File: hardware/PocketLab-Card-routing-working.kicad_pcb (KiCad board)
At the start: 4 copper layers, 85.6 x 54 mm, 260 parts, among them J1 USB-C DATA/POWER, J2 microSD, J3 EXTERNAL 400uH LF COIL, J4 PROTECTED 1S LiPo 3.7V, J5 30-PIN 2.54mm DUPONT GRID, Q1 AO3400A IR DRIVER, Q2 CSD16406Q3 DISCHARGE, Q3 CSD16406Q3 CHARGE, SW1 RESET, SW2 BOOT, SW3 UP, SW4 DOWN, SW5 MAIN POWER OFF / ON, SW6 PAIR, SW7 SELECT, SW8 AUX CONFIG, U1 ESP32-S3-WROOM-1-N8R2, U10 BMI270 (FULL OPTION), U11 BMP390 (FULL OPTION), U12 PCF8563T, U13 TSOP75338WTR 38kHz, U14 BQ29700DSE, U15 TPS2553DBVR 500mA LIMIT, U16 USBLC6-4SC6Y, U17 TPS22919DCKR LF 5V LOAD SWITCH, U18 TCA9534PWR INTERNAL CONTROL, U19 SRV05-4MR6T1G SD ESD, U2 PN5321A3HN/C106, U20 SN74AHCT1G126DBVR RGB LEVEL S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, U21 SN74LV125ATPWR LF/SPI 3V3-TO-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, U22 SN74LVC1G126DBVR LF 5V-TO-3V3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, U23 ATECC608C-SSHDA-T, U24 SRV05-4MR6T1G J5 BUS ESD, U25 SRV05-4MR6T1G J5 SPI ESD, U3 E07-900MM10S 855-925MHz, U4 HTRC11001T/03EE,11 125kHz, U5 BQ24074RGTR, U6 TPS63070RNMR 3V3, U7 TPS61023DRLR 5V BOOST, U8 MAX17048G+T10, U9 TCA9535PWR, Y301 27.12MHz crystal (pins 2/4 sh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, Y501 4MHz 5V CMOS OSCILLATOR, Y701 32.768kHz CL=7pF

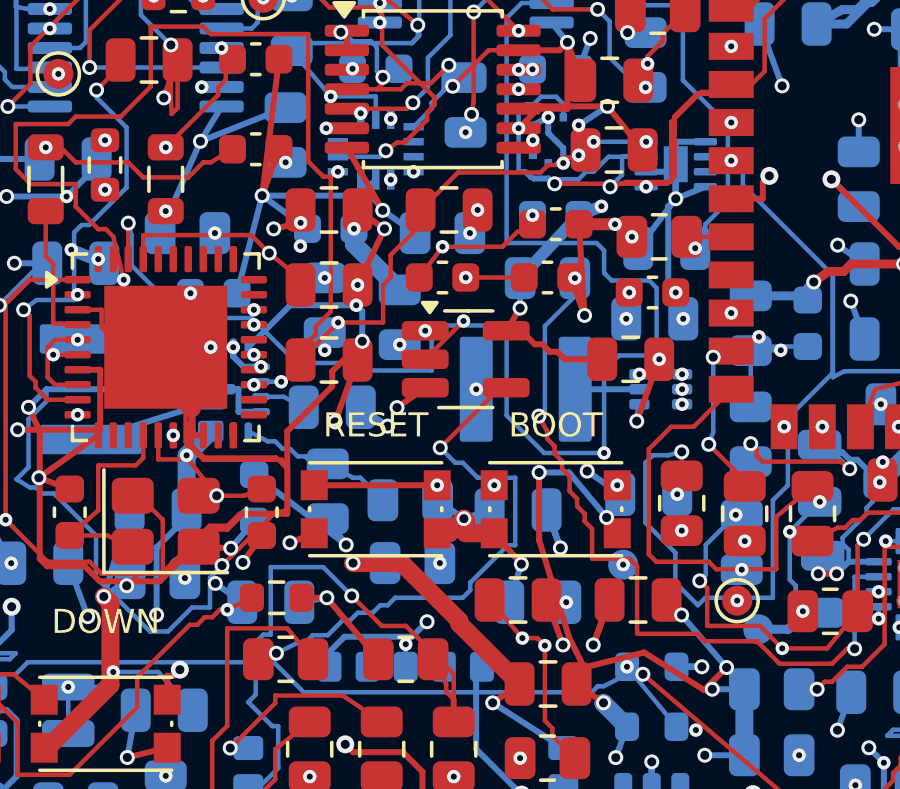
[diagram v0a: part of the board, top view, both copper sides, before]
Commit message: Reduce routing conflicts around power and control nets
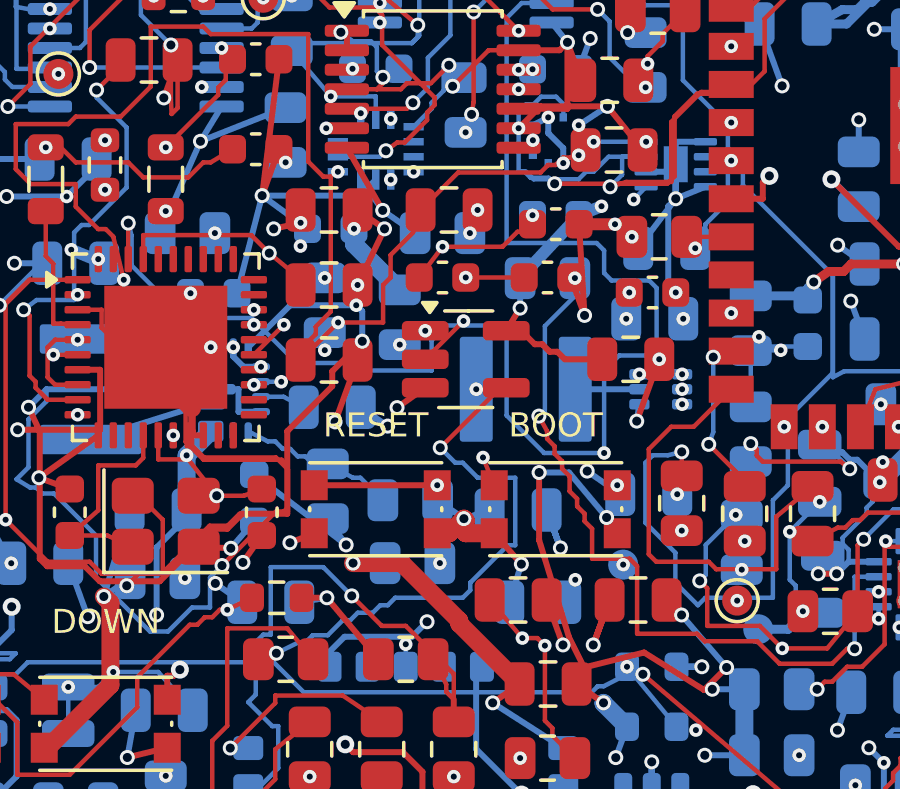
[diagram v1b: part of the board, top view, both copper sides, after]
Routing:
- net /BQ_EN1: track 47.3 -> 58.1 mm
- net /BOARD_TEMP_HDR: track 74.7 -> 78.7 mm
- net /BOOT_N: track 76.7 -> 78.6 mm
- net /+5V_RAW: track 227.8 -> 229.0 mm
- net /FG_ALERT_N: track 25.1 -> 26.1 mm
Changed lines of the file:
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@@
 	)
 	(via
-		(at 78.35 51.1)
+		(at 78.65 50.35)
 		(size 0.45)
 		(drill 0.2)
@@
 	)
 	(segment
-		(start 78.35 51.1)
+		(start 78.65 50.35)
 		(end 82.6715 55.3622)
 		(width 0.4)
@@
 	)
 	(segment
+		(start 78.35 51.1)
+		(end 78.65 50.35)
+		(width 0.4)
+		(locked yes)
+		(layer "B.Cu")
+		(net "/+5V_RAW")
+	)
+	(segment
 		(start 49.4104 59.75)
 		(end 48.4557 60.7047)
@@
 		(width 0.15)
 		(locked yes)
-		(layer "In1.Cu")
+		(layer "In2.Cu")
 		(net "/ESP_EN")
 	)
@@
 		(net "/I2C_SCL")
 	)
+	(segment
+		(start 67.9375 42.85)
+		(end 68.9375 41.85)
+		(width 0.15)
+		(layer "F.Cu")
+		(net "/NFC_IRQ_N")
+	)
 	(via
 		(at 83.85 35.11)
@@
 	)
 	(via
-		(at 67.9375 42.85)
+		(at 68.9375 41.85)
 		(size 0.45)
 		(drill 0.2)
@@
 	)
 	(segment
-		(start 67.9375 42.85)
+		(start 68.9375 41.85)
 		(end 83.85 35.11)
 		(width 0.15)
@@
 	)
 	(via
-		(at 75.95 47.2)
+		(at 75.575 46.275)
 		(size 0.45)
 		(drill 0.2)
@@
 	)
 	(segment
-		(start 75.95 47.2)
+		(start 75.575 46.275)
 		(end 75.95 62)
 		(width 0.15)
@@
 	)
 	(segment
+		(start 75.95 47.2)
+		(end 75.575 46.275)
+		(width 0.15)
+		(locked yes)
+		(layer "F.Cu")
+		(net "/BOOT_N")
+	)
+	(segment
 		(start 66.2 65.7125)
 		(end 65.65 65.7125)
@@
 	)
 	(segment
-		(start 59.2 23.2)
+		(start 61.2 52.8)
 		(end 59.2 52.8)
 		(width 0.15)
@@
 	)
 	(segment
+		(start 61.2 23.2)
+		(end 61.2 52.8)
+		(width 0.15)
+		(locked yes)
+		(layer "In2.Cu")
+		(net "/BOARD_TEMP_HDR")
+	)
+	(segment
+		(start 59.2 23.2)
+		(end 61.2 23.2)
+		(width 0.15)
+		(locked yes)
+		(layer "In2.Cu")
+		(net "/BOARD_TEMP_HDR")
+	)
+	(segment
 		(start 30.575 21.82)
 		(end 30.575 23.2)
@@
 	(segment
 		(start 88.7625 50.75)
+		(end 90 50.75)
+		(width 0.15)
+		(locked yes)
+		(layer "In2.Cu")
+		(net "/BQ_EN1")
+	)
+	(segment
+		(start 90 50.75)
+		(end 90 29.175)
+		(width 0.15)
+		(locked yes)
+		(layer "In2.Cu")
+		(net "/BQ_EN1")
+	)
+	(segment
+		(start 90 29.175)
 		(end 77.8625 29.175)
 		(width 0.15)
@@
 	)
 	(via
-		(at 81.0125 37.25)
+		(at 80.6 37.675)
 		(size 0.45)
 		(drill 0.2)
@@
 	)
 	(segment
-		(start 81.0125 37.25)
+		(start 80.6 37.675)
 		(end 80.995 33.9375)
 		(width 0.15)
@@
 		(net "/FG_ALERT_N")
 	)
+	(segment
+		(start 81.0125 37.25)
+		(end 80.6 37.675)
+		(width 0.15)
+		(locked yes)
+		(layer "B.Cu")
+		(net "/FG_ALERT_N")
+	)

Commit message: Close final ground island and reduce inner-layer conflicts
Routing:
- net /GND: track 761.0 -> 764.8 mm

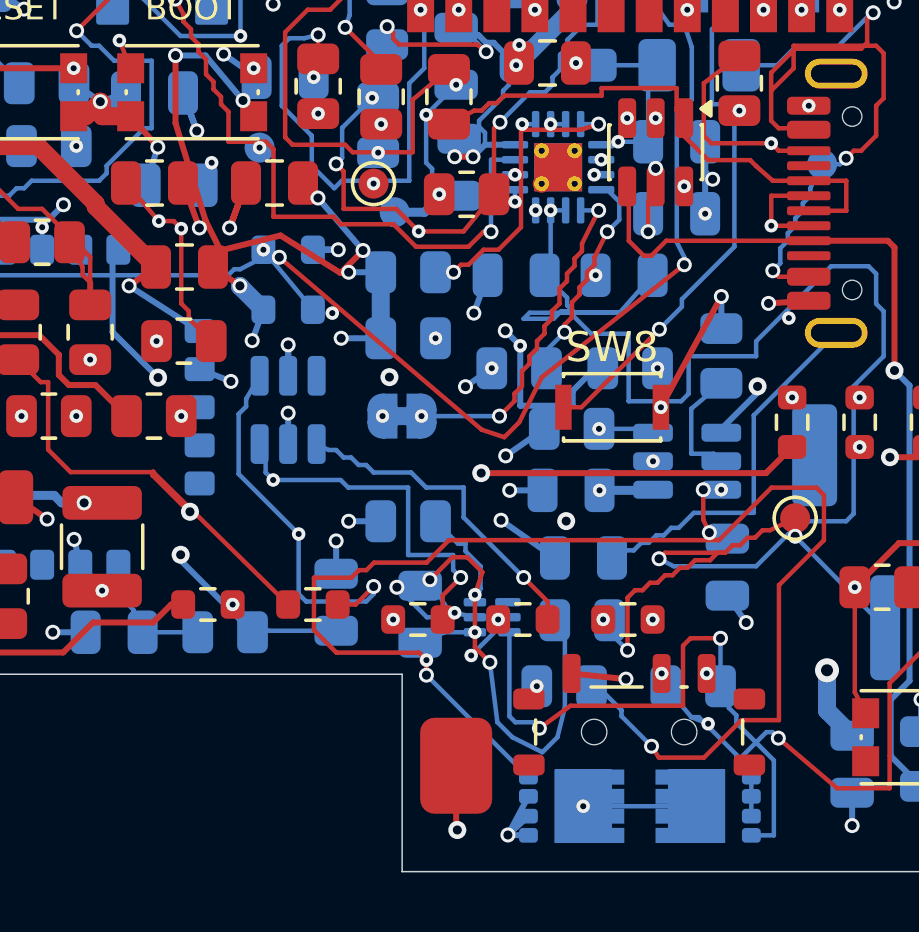
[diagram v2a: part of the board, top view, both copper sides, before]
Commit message: Reduce major hole-clearance routing clusters
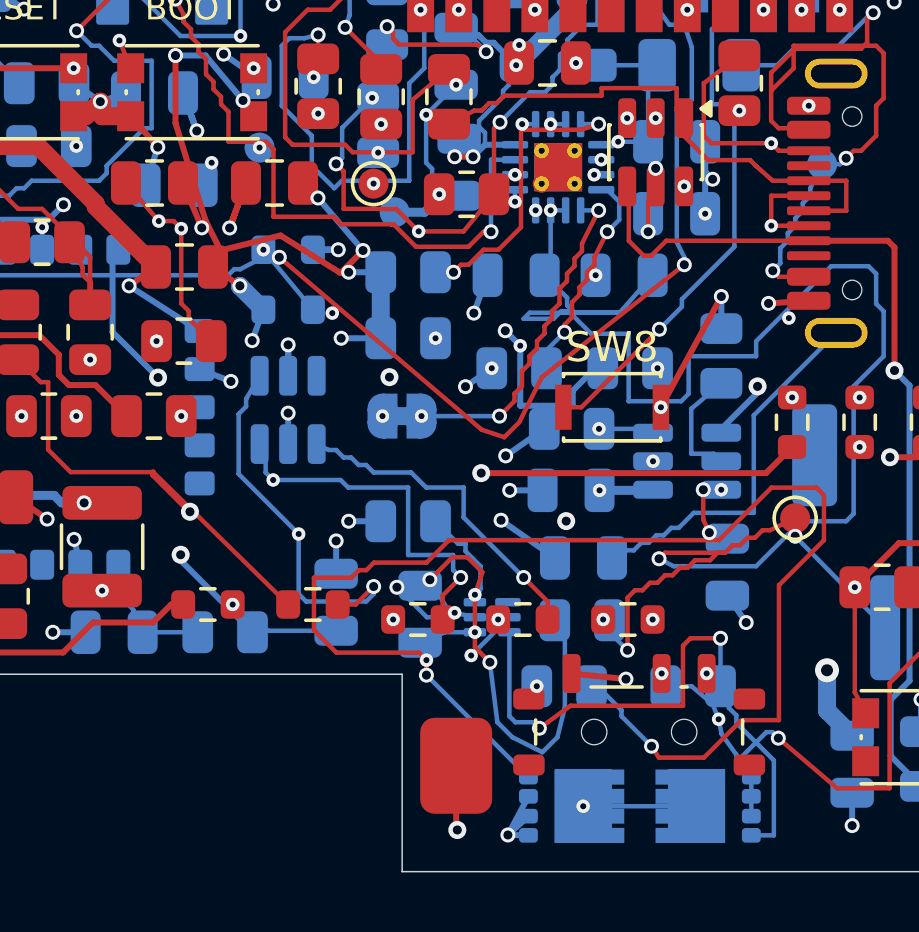
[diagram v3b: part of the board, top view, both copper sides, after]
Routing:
- net /LF_SCLK_5V: track 43.0 -> 45.8 mm
- net /LF_5V: track 70.2 -> 71.5 mm
- net /EX6: track 65.0 -> 65.6 mm
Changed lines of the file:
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@@
 	(segment
 		(start 77.695 51.025)
-		(end 78.2405 52.5238)
+		(end 78.32 52.52)
 		(width 0.2)
 		(layer "F.Cu")
@@
 	)
 	(via
-		(at 78.2405 52.5238)
+		(at 78.32 52.52)
 		(size 0.5)
 		(drill 0.3)
@@
 	(segment
 		(start 61.75 53.925)
+		(end 60.8 52.8)
+		(width 0.15)
+		(locked yes)
+		(layer "In2.Cu")
+		(net "/LF_5V")
+	)
+	(segment
+		(start 60.8 52.8)
+		(end 57.5 52.8)
+		(width 0.15)
+		(locked yes)
+		(layer "In2.Cu")
+		(net "/LF_5V")
+	)
+	(segment
+		(start 57.5 52.8)
+		(end 46.569 56.85)
+		(width 0.15)
+		(locked yes)
+		(layer "In2.Cu")
+		(net "/LF_5V")
+	)
+	(segment
+		(start 46.569 56.85)
 		(end 45.1625 58.25)
 		(width 0.15)
@@
 	(segment
 		(start 59.6 53.41)
+		(end 59.6 51)
+		(width 0.15)
+		(locked yes)
+		(layer "In2.Cu")
+		(net "/LF_SCLK_5V")
+	)
+	(segment
+		(start 59.6 51)
+		(end 61.4 50)
+		(width 0.15)
+		(locked yes)
+		(layer "In2.Cu")
+		(net "/LF_SCLK_5V")
+	)
+	(segment
+		(start 61.4 50)
+		(end 61.4 35.3)
+		(width 0.15)
+		(locked yes)
+		(layer "In2.Cu")
+		(net "/LF_SCLK_5V")
+	)
+	(segment
+		(start 61.4 35.3)
 		(end 59.6 35.3)
 		(width 0.15)
@@
 	(segment
 		(start 60 22.4)
+		(end 60 38)
+		(width 0.15)
+		(locked yes)
+		(layer "In2.Cu")
+		(net "/EX6")
+	)
+	(segment
+		(start 60 38)
+		(end 60.9 39)
+		(width 0.15)
+		(locked yes)
+		(layer "In2.Cu")
+		(net "/EX6")
+	)
+	(segment
+		(start 60.9 39)
+		(end 60.9 50.5)
+		(width 0.15)
+		(locked yes)
+		(layer "In2.Cu")
+		(net "/EX6")
+	)
+	(segment
+		(start 60.9 50.5)
+		(end 60 51.5)
+		(width 0.15)
+		(locked yes)
+		(layer "In2.Cu")
+		(net "/EX6")
+	)
+	(segment
+		(start 60 51.5)
 		(end 60 52.8)
 		(width 0.15)
@@
 	)
 	(via
-		(at 95.2 69.05)
+		(at 95.55 68.9)
 		(size 0.45)
 		(drill 0.2)
@@
 	)
 	(segment
+		(start 94.65 67.8)
+		(end 95.35 68.4)
+		(width 0.15)
+		(layer "B.Cu")
+		(net "/CELL_NEG")
+	)
+	(segment
 		(start 96.64 71.47)
 		(end 96.64 70.83)
@@
 	)
 	(segment
-		(start 96.14 70.08)
-		(end 94.89 68.83)
+		(start 93.7875 67.8)
+		(end 94.65 67.8)
 		(width 0.15)
 		(layer "B.Cu")
@@
 	)
 	(segment
-		(start 94.64 68.83)
-		(end 93.7875 67.8)
+		(start 95.35 68.4)
+		(end 95.55 68.9)
 		(width 0.15)
 		(layer "B.Cu")
@@
 	)
 	(segment
-		(start 94.89 68.83)
-		(end 94.64 68.83)
+		(start 96.64 71.47)
+		(end 96.64 72.13)
 		(width 0.15)
 		(layer "B.Cu")
@@
 	)
 	(segment
-		(start 96.64 71.47)
-		(end 96.64 72.13)
+		(start 86.425 66)
+		(end 85.6 66.35)
 		(width 0.15)
 		(layer "B.Cu")
@@
 	)
 	(segment
-		(start 86.425 66)
-		(end 85.6 66.35)
+		(start 95.55 68.9)
+		(end 95.65 69.4)
 		(width 0.15)
 		(layer "B.Cu")
@@
 	)
 	(segment
+		(start 95.65 69.4)
+		(end 96.14 70.08)
+		(width 0.15)
+		(layer "B.Cu")
+		(net "/CELL_NEG")
+	)
+	(segment
 		(start 97.14 69.33)
 		(end 96.14 70.33)
@@
 	)
 	(segment
-		(start 94.64 68.83)
-		(end 95.2 69.05)
-		(width 0.15)
-		(locked yes)
-		(layer "B.Cu")
-		(net "/CELL_NEG")
-	)
-	(segment
 		(start 87.425 66)
-		(end 95.2 69.05)
+		(end 95.55 68.9)
 		(width 0.15)
 		(locked yes)

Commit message: Reroute additional inner-layer hole conflicts
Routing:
- net /BOARD_TEMP_HDR: track 78.7 -> 79.3 mm
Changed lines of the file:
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@@
 	(segment
 		(start 54.73 64.459999)
+		(end 59.181 63.002)
+		(width 0.15)
+		(locked yes)
+		(layer "In1.Cu")
+		(net "/GPIO41")
+	)
+	(segment
+		(start 59.181 63.002)
+		(end 95.597 59.294)
+		(width 0.15)
+		(locked yes)
+		(layer "In1.Cu")
+		(net "/GPIO41")
+	)
+	(segment
+		(start 95.597 59.294)
 		(end 100.25 59.825)
 		(width 0.15)
@@
 	(segment
 		(start 30.575 23.2)
+		(end 31.5 22.4)
+		(width 0.15)
+		(locked yes)
+		(layer "In2.Cu")
+		(net "/BOARD_TEMP_HDR")
+	)
+	(segment
+		(start 31.5 22.4)
+		(end 58.3 22.4)
+		(width 0.15)
+		(locked yes)
+		(layer "In2.Cu")
+		(net "/BOARD_TEMP_HDR")
+	)
+	(segment
+		(start 58.3 22.4)
 		(end 59.2 23.2)
 		(width 0.15)
@@
 	(segment
 		(start 74.995 35.4375)
+		(end 77.193 36.429)
+		(width 0.15)
+		(locked yes)
+		(layer "In2.Cu")
+		(net "/CHG_DISABLE")
+	)
+	(segment
+		(start 77.193 36.429)
+		(end 88.756 49.629)
+		(width 0.15)
+		(locked yes)
+		(layer "In2.Cu")
+		(net "/CHG_DISABLE")
+	)
+	(segment
+		(start 88.756 49.629)
 		(end 89.45 51.9375)
 		(width 0.15)

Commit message: Resolve SPI overlap and reroute GPIO8
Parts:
- moved C704 0.50 mm to (78.5, 33.3)
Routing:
- net /GPIO8: track 78.7 -> 79.3 mm
- net /+3V3: track 392.6 -> 392.0 mm
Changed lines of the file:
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@@
 	(footprint "Capacitor_SMD:C_0603_1608Metric"
 		(layer "B.Cu")
-		(at 78 33.335)
+		(at 78.5 33.335)
 		(descr "Capacitor SMD 0603 (1608 Metric), square (rectangular) end terminal, IPC-7351 nominal, (Body size source: IPC-SM-782 page 76, https://www.pcb-3d.com/wordpress/wp-content/uploads/ipc-sm-782a_amendment_1_and_2.pdf)")
 		(tags "capacitor")
@@
 	)
 	(segment
-		(start 78.775 33.335)
+		(start 79.275 33.335)
 		(end 79.1495 32.306)
 		(width 0.2)
@@
 	)
 	(via
-		(at 77.225 33.335)
+		(at 77.725 33.335)
 		(size 0.45)
 		(drill 0.2)
@@
 	)
 	(segment
-		(start 77.225 33.335)
+		(start 77.725 33.335)
 		(end 87.3988 32.112499)
 		(width 0.4)
@@
 	(segment
 		(start 77.75 34.9375)
-		(end 77.225 33.335)
+		(end 77.725 33.335)
 		(width 0.4)
 		(locked yes)
@@
 	(segment
 		(start 21.7 52.8)
+		(end 22.5 53.78)
+		(width 0.15)
+		(locked yes)
+		(layer "In1.Cu")
+		(net "/GPIO8")
+	)
+	(segment
+		(start 22.5 53.78)
+		(end 61.5 62.53)
+		(width 0.15)
+		(locked yes)
+		(layer "In1.Cu")
+		(net "/GPIO8")
+	)
+	(segment
+		(start 61.5 62.53)
 		(end 62.35 61.92)
 		(width 0.15)

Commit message: Reroute inner signals around drill conflicts
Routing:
- net /GPIO1: track 59.8 -> 62.2 mm
- net /U6_PS_SYNC: track 42.9 -> 44.8 mm
- net /STRAP_BOOT_TP: track 23.5 -> 25.0 mm
- net /IR_TX: track 43.8 -> 45.0 mm
